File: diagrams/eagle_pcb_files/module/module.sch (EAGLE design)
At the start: 3 parts

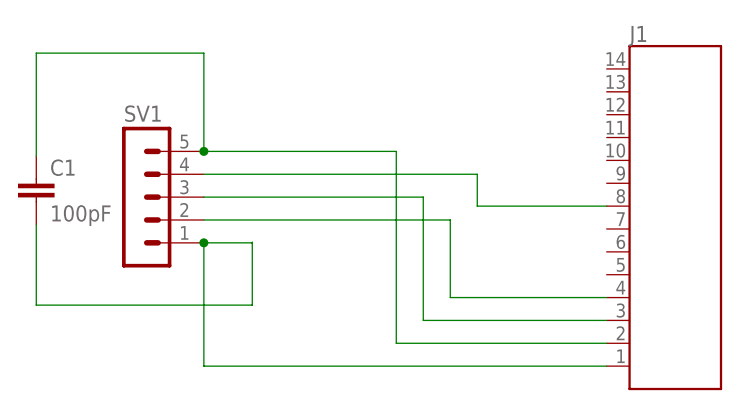
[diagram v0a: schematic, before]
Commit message: small fixes, 100pF -> 100nF, tht cap to smd cap, mounting holes, round dimension, one sided instead of two sided, gnd plane
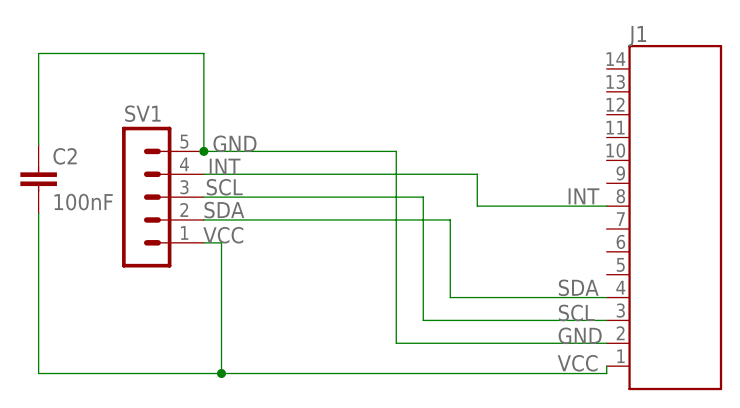
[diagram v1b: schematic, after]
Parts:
- removed C1: 100pF, capacitor-wima:C2,5-3
- added C2: 100nF, eagle-ltspice:CC1206
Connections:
- net N$3 renamed SCL
- net N$4 renamed SDA
- net N$5 renamed INT
- removed net N$1: C1.2, J1.14, SV1.1
- removed net N$2: C1.1, J1.13, SV1.5
- new net GND: C2.1, J1.13, SV1.5
- new net VCC: C2.2, J1.14, SV1.1
